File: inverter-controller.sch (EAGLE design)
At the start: 140 parts, among them IC1 STM32F334C8T6, IC10 ISO3082, IC2 SY7152ABC, IC3 LMV358MMX, IC4 LMV358MMX, J1 621006245821, J2 61300211121, X1 0289-9066**15EDGVC-3.81-02P-14, X2 0289-9066**15EDGVC-3.81-02P-14, X3 0289-9068**15EDGVC-3.81-03P-14, X6 1365-16, Y1 NX2016SA-32M

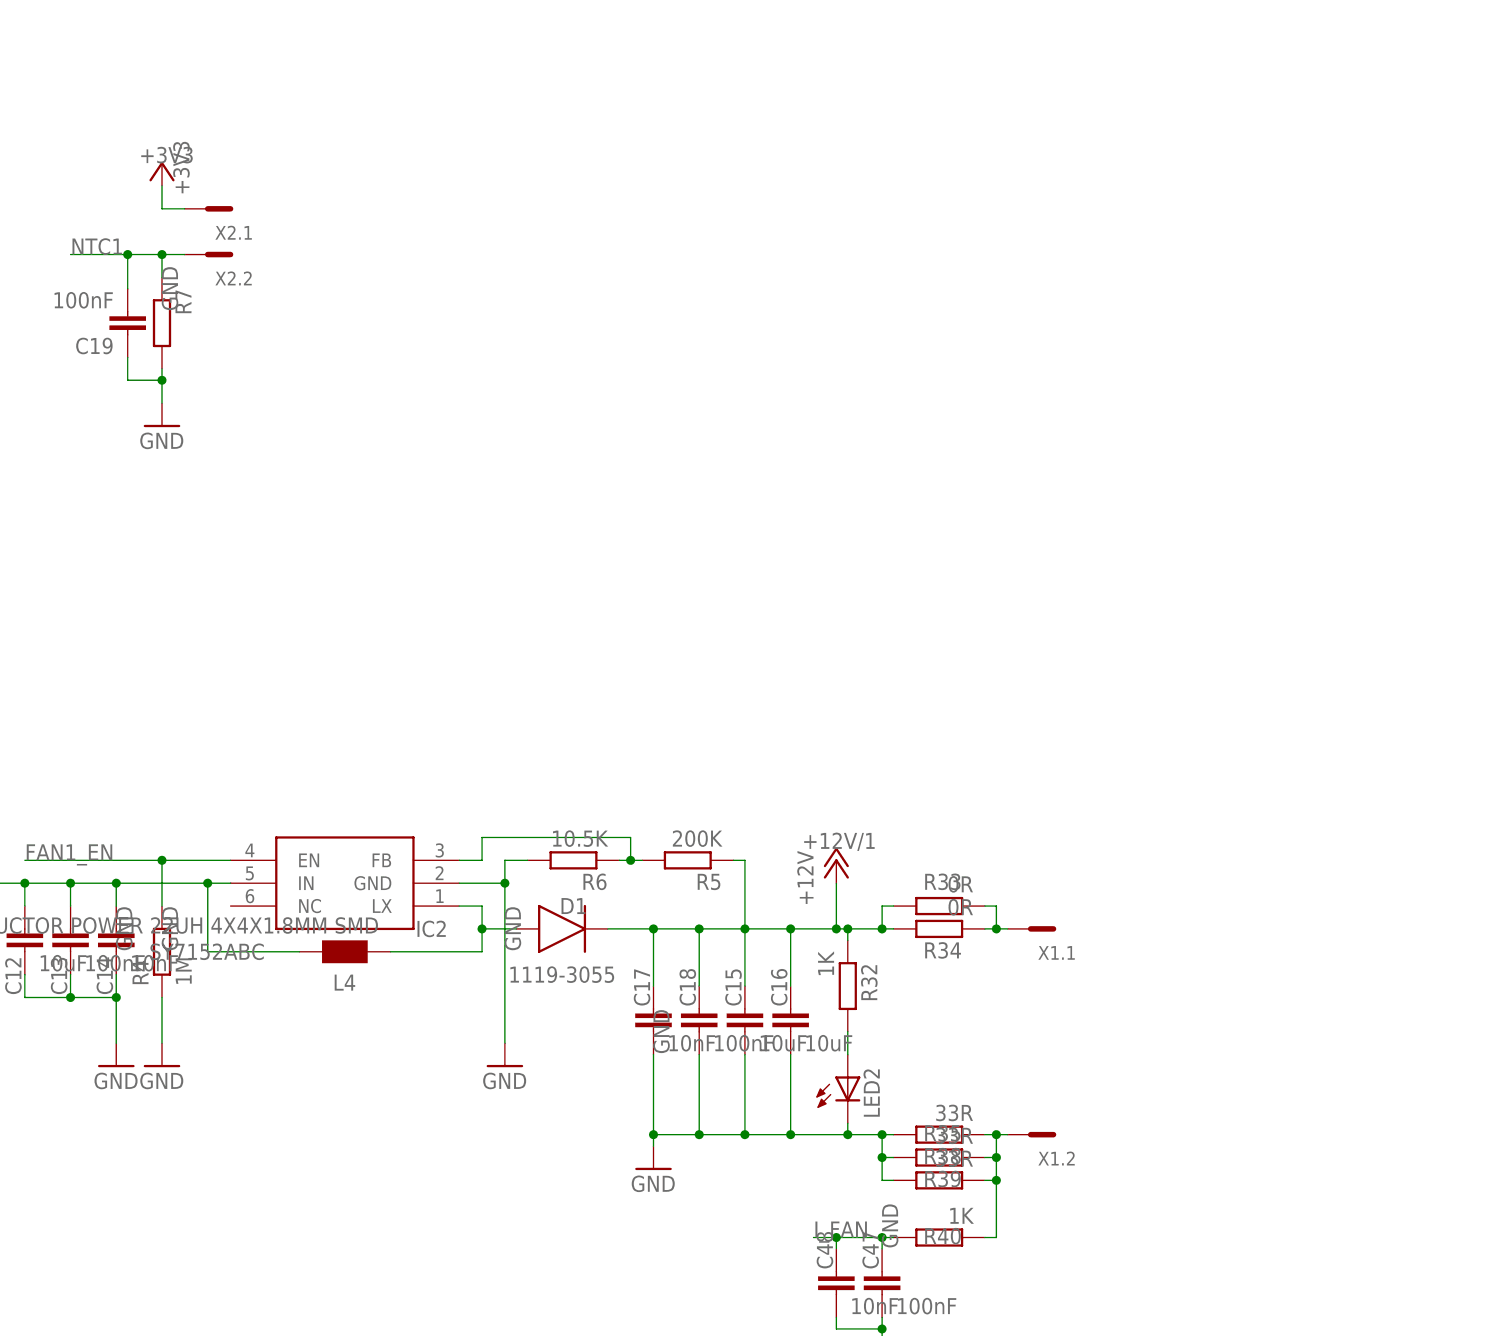
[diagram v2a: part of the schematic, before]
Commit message: Fan ve NTC soketleri SMD-Pad kutuphanesi ile degistirildi.
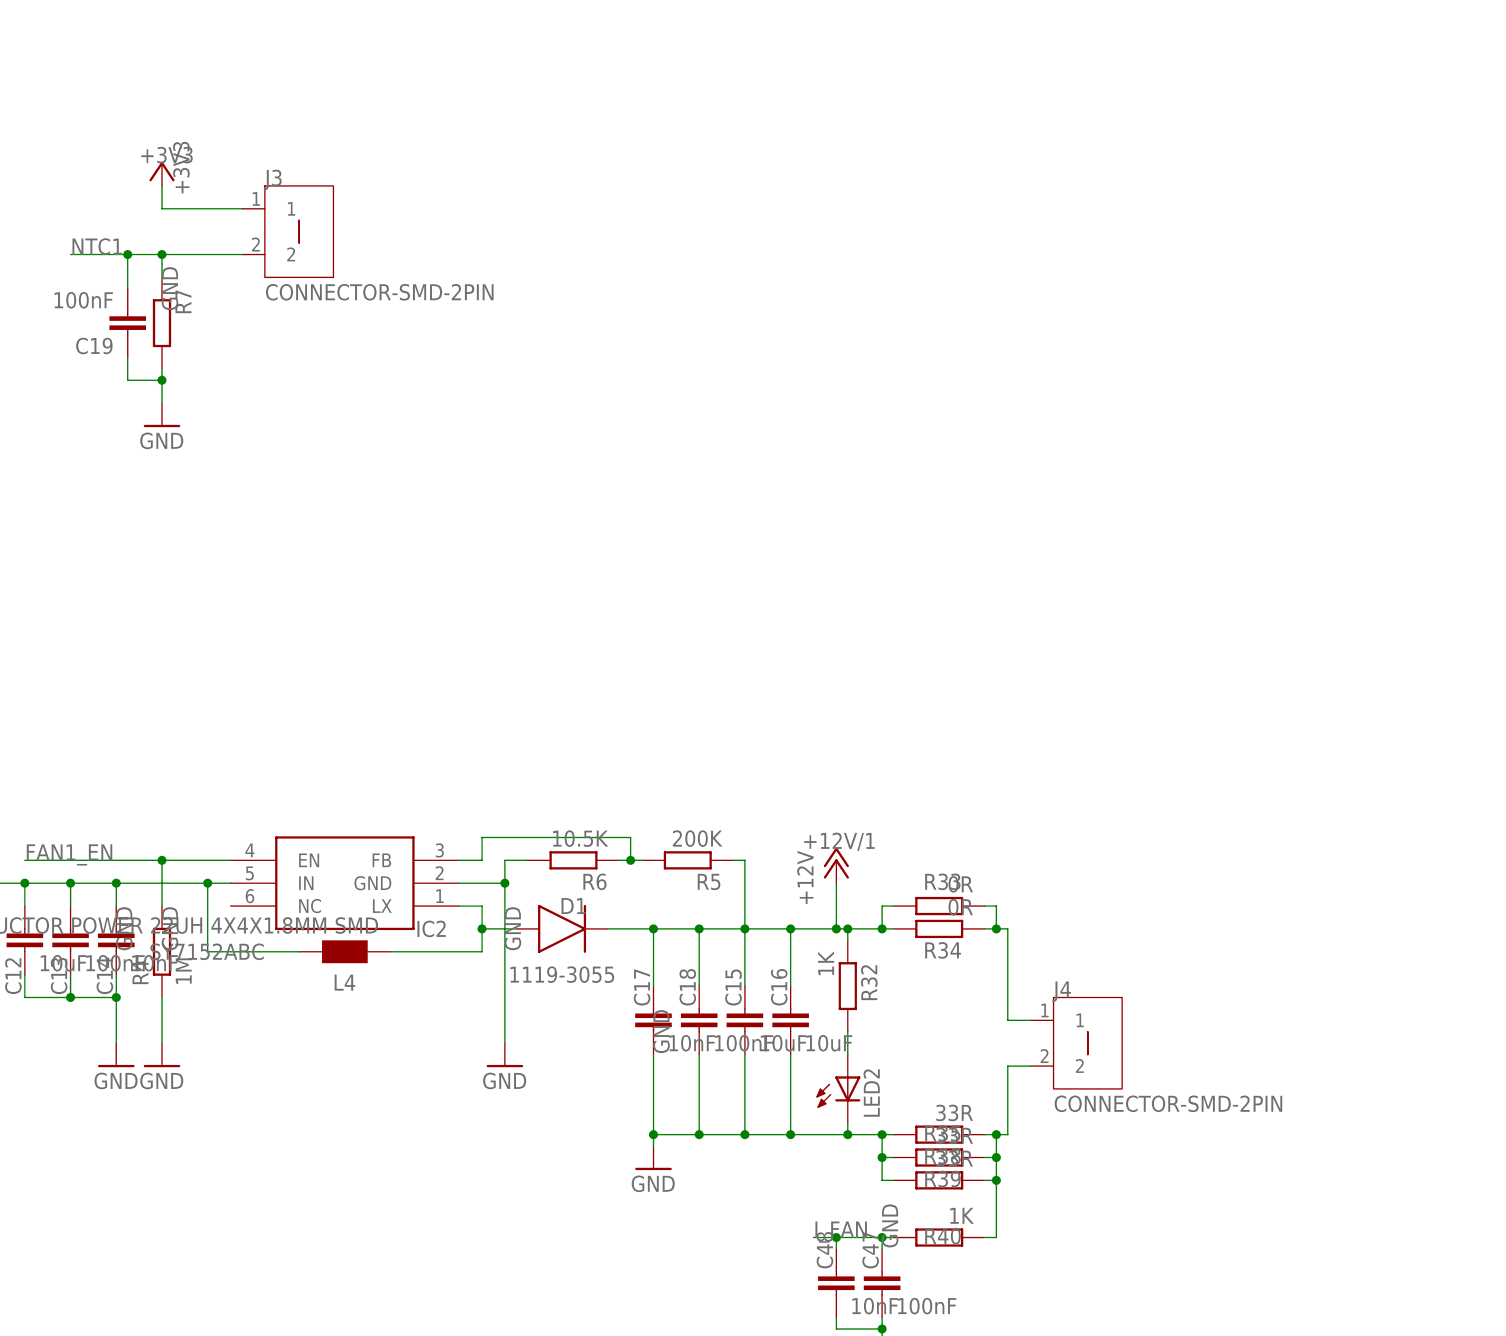
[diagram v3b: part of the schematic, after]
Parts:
- removed X1, X2: 0289-9066**15EDGVC-3.81-02P-14, con-phoenix-381_l:MCV2
- added J3, J4: CONNECTOR-SMD-2PIN, Andromeda:CONNECTOR-SMD-2PIN
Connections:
- net +3V3: now also J3.1; no longer X2.1.SK
- net N$10: now also J4.2; no longer X1.2.SK
- net N$34: now also J4.1; no longer X1.1.SK
- net NTC1: now also J3.2; no longer X2.2.SK
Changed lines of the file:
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@@
 <part name="GND12" library="supply1" library_urn="urn:adsk.eagle:library:371" deviceset="GND" device=""/>
 <part name="P+1" library="supply1" library_urn="urn:adsk.eagle:library:371" deviceset="+12V" device=""/>
-<part name="X1" library="con-phoenix-381_l" deviceset="MCV2" device="" value="0289-9066**15EDGVC-3.81-02P-14"/>
-<part name="X2" library="con-phoenix-381_l" deviceset="MCV2" device="" value="0289-9066**15EDGVC-3.81-02P-14"/>
 <part name="+3V7" library="supply1" library_urn="urn:adsk.eagle:library:371" deviceset="+3V3" device=""/>
 <part name="GND14" library="supply1" library_urn="urn:adsk.eagle:library:371" deviceset="GND" device=""/>
@@
 <part name="+3V17" library="supply1" deviceset="+3V3" device=""/>
 <part name="DC7" library="my_parts1" deviceset="RI-0512S/P_DC_DC_5V_12V" device=""/>
+<part name="J3" library="Andromeda" library_urn="urn:adsk.eagle:library:27258842" deviceset="CONNECTOR-SMD-2PIN" device=""/>
+<part name="J4" library="Andromeda" library_urn="urn:adsk.eagle:library:27258842" deviceset="CONNECTOR-SMD-2PIN" device=""/>
 </parts>
 <sheets>
@@
 <attribute name="VALUE" x="321.31" y="21.59" size="1.778" layer="96" rot="R90"/>
 </instance>
-<instance part="X1" gate=".1" x="342.9" y="19.05" smashed="yes" rot="R180">
-<attribute name="NAME" x="350.52" y="17.145" size="1.524" layer="95" rot="R180"/>
-</instance>
-<instance part="X1" gate=".2" x="342.9" y="-3.81" smashed="yes" rot="R180">
-<attribute name="NAME" x="350.52" y="-5.715" size="1.524" layer="95" rot="R180"/>
-</instance>
-<instance part="X2" gate=".1" x="251.46" y="99.06" smashed="yes" rot="R180">
-<attribute name="NAME" x="259.08" y="97.155" size="1.524" layer="95" rot="R180"/>
-</instance>
-<instance part="X2" gate=".2" x="251.46" y="93.98" smashed="yes" rot="R180">
-<attribute name="NAME" x="259.08" y="92.075" size="1.524" layer="95" rot="R180"/>
-</instance>
 <instance part="+3V7" gate="G$1" x="248.92" y="104.14" smashed="yes">
 <attribute name="VALUE" x="250.19" y="106.68" size="1.778" layer="96" rot="R270"/>
@@
 <attribute name="NAME" x="403.86" y="172.72" size="1.778" layer="95"/>
 <attribute name="VALUE" x="403.86" y="158.75" size="1.778" layer="96"/>
+</instance>
+<instance part="J3" gate="G$1" x="262.89" y="96.52" smashed="yes">
+<attribute name="VALUE" x="260.35" y="88.9" size="1.778" layer="96"/>
+<attribute name="NAME" x="260.35" y="101.6" size="1.778" layer="95"/>
+</instance>
+<instance part="J4" gate="G$1" x="350.52" y="6.35" smashed="yes">
+<attribute name="VALUE" x="347.98" y="-1.27" size="1.778" layer="96"/>
+<attribute name="NAME" x="347.98" y="11.43" size="1.778" layer="95"/>
 </instance>
 </instances>
@@
 </segment>
 <segment>
-<pinref part="X2" gate=".1" pin="SK"/>
-<wire x1="251.46" y1="99.06" x2="248.92" y2="99.06" width="0.1524" layer="91"/>
 <pinref part="+3V7" gate="G$1" pin="+3V3"/>
 <wire x1="248.92" y1="99.06" x2="248.92" y2="101.6" width="0.1524" layer="91"/>
 <label x="246.38" y="104.14" size="1.778" layer="95"/>
+<pinref part="J3" gate="G$1" pin="1"/>
+<wire x1="248.92" y1="99.06" x2="257.81" y2="99.06" width="0.1524" layer="91"/>
 </segment>
 <segment>
@@
 </segment>
 <segment>
-<pinref part="X2" gate=".2" pin="SK"/>
-<wire x1="251.46" y1="93.98" x2="248.92" y2="93.98" width="0.1524" layer="91"/>
 <wire x1="248.92" y1="93.98" x2="245.11" y2="93.98" width="0.1524" layer="91"/>
 <wire x1="245.11" y1="93.98" x2="238.76" y2="93.98" width="0.1524" layer="91"/>
@@
 <junction x="248.92" y="93.98"/>
 <pinref part="C19" gate="G$1" pin="2"/>
+<pinref part="J3" gate="G$1" pin="2"/>
+<wire x1="248.92" y1="93.98" x2="257.81" y2="93.98" width="0.1524" layer="91"/>
 </segment>
 </net>
@@
 <net name="N$34" class="0">
 <segment>
-<pinref part="X1" gate=".1" pin="SK"/>
 <wire x1="340.36" y1="19.05" x2="341.63" y2="19.05" width="0.1524" layer="91"/>
 <wire x1="341.63" y1="19.05" x2="342.9" y2="19.05" width="0.1524" layer="91"/>
@@
 <pinref part="R33" gate="G$1" pin="1"/>
 <pinref part="R34" gate="G$1" pin="1"/>
+<wire x1="342.9" y1="19.05" x2="342.9" y2="8.89" width="0.1524" layer="91"/>
+<pinref part="J4" gate="G$1" pin="1"/>
+<wire x1="342.9" y1="8.89" x2="345.44" y2="8.89" width="0.1524" layer="91"/>
 </segment>
 </net>
 <net name="N$10" class="0">
 <segment>
-<pinref part="X1" gate=".2" pin="SK"/>
 <wire x1="340.36" y1="-3.81" x2="341.63" y2="-3.81" width="0.1524" layer="91"/>
 <wire x1="341.63" y1="-3.81" x2="342.9" y2="-3.81" width="0.1524" layer="91"/>
@@
 <pinref part="R39" gate="G$1" pin="1"/>
 <pinref part="R40" gate="G$1" pin="1"/>
-</segment>
-</net>
+<pinref part="J4" gate="G$1" pin="2"/>
+<wire x1="345.44" y1="3.81" x2="342.9" y2="3.81" width="0.1524" layer="91"/>
+<wire x1="342.9" y1="3.81" x2="342.9" y2="-3.81" width="0.1524" layer="91"/>
+</segment>
+</net>

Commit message: 485 pinleri degistirildi, analog-girisler icin aciklama eklendi.
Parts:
- added C54, C59, C62: 10uF, rcl:C-EUC0603E
- added C55, C58, C63: 100nF, rcl:C-EUC0603E
- added C56, C57, C64: 10nF, rcl:C-EUC0603E
- added D5: 1119-3055, Diode:DIODEDO-214AC(SMA)
- added IC5: SY7152ABC, SY7152ABC:SY7152ABC
- added J5: CONNECTOR-SMD-2PIN, Andromeda:CONNECTOR-SMD-2PIN
- added L2: 1319-4102**INDUCTOR POWER 22UH 4X4X1.8MM SMD, wuerth-elektronik:WE-PD2_S
- added LED3: (no value), adafruit:LEDCHIP-LED0805
- added R42: 1M, rcl:R-EU_R0603E
- added R43: 200K, rcl:R-EU_R0603E
- added R44: 10.5K, rcl:R-EU_R0603E
- added R45, R46: 0R, rcl:R-EU_R0603E
- added R47, R55: 1K, rcl:R-EU_R0603E
- added R49, R50, R53: 33R, rcl:R-EU_R0603E
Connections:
- new net +12V/2: C57.1, C58.1, C59.1, C62.1, D5.C, R43.1, R45.2, R46.2, R47.1
- new net FAN2_EN: IC1.PB13, IC5.EN, R42.2
- new net I_FAN1: C47.1, C48.1, R40.2
- new net N$25: D5.A, IC5.LX, L2.1
- new net N$26: IC5.FB, R43.2, R44.1
- new net N$27: J5.1, R45.1, R46.1
- new net N$28: J5.2, R49.1, R50.1, R53.1, R55.1
- new net N$29: LED3.A, R47.2
- net +3V3: now also C54.1, C55.1, C56.1, IC5.IN, L2.2
- net GND: now also C54.2, C55.2, C56.2, C57.2, C58.2, C59.2, C62.2, C63.2, C64.2, IC5.GND, LED3.C, R42.1, R44.2, R49.2, R50.2, R53.2
- net I_FAN: now also C63.1, C64.1, R55.2; no longer C47.1, C48.1, R40.2
- net RS485_RX: now also IC1.PB7; no longer IC1.PB11
- net RS485_TX: now also IC1.PB6; no longer IC1.PB10
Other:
- note added: "/ADC2_IN13"
- note added: "/ADC2_IN14"
- note added: "/ADC2_IN15"
- note added: "ADC1_IN11/"
- note added: "ADC1_IN12/"
- note added: "ADC2_IN12/"

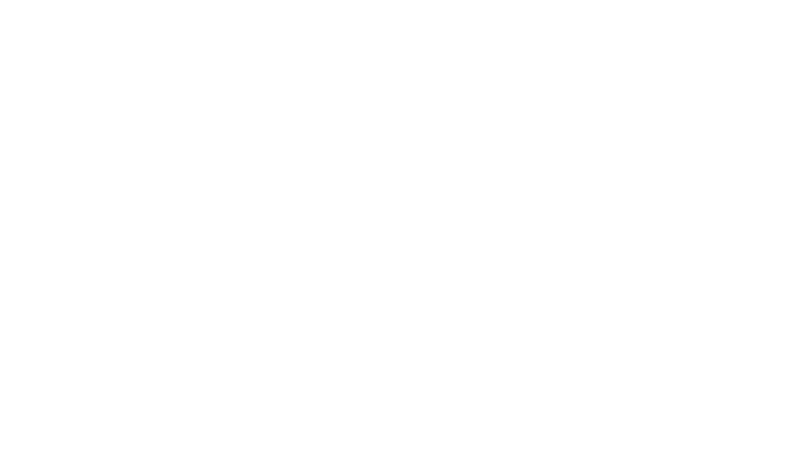
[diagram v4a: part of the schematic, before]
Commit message: Kart baglanti pad'leri eklendi.
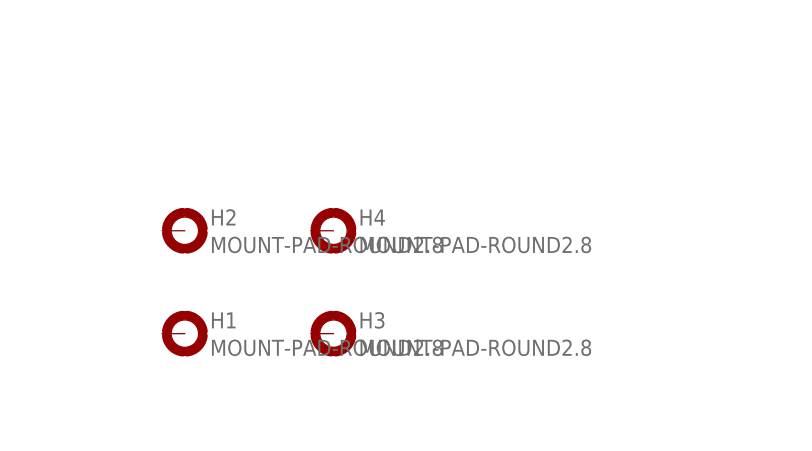
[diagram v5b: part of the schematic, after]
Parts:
- added H1, H2, H3, H4: MOUNT-PAD-ROUND2.8, holes:MOUNT-PAD-ROUND2.8
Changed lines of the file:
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@@
 <part name="C64" library="rcl" library_urn="urn:adsk.eagle:library:26637914" deviceset="C-EU" device="C0603E" package3d_urn="urn:adsk.eagle:package:26638827/1" value="10nF"/>
 <part name="J5" library="Andromeda" library_urn="urn:adsk.eagle:library:27258842" deviceset="CONNECTOR-SMD-2PIN" device=""/>
+<part name="H1" library="holes" library_urn="urn:adsk.eagle:library:237" deviceset="MOUNT-PAD-ROUND" device="2.8" package3d_urn="urn:adsk.eagle:package:14281/1"/>
+<part name="H2" library="holes" library_urn="urn:adsk.eagle:library:237" deviceset="MOUNT-PAD-ROUND" device="2.8" package3d_urn="urn:adsk.eagle:package:14281/1"/>
+<part name="H3" library="holes" library_urn="urn:adsk.eagle:library:237" deviceset="MOUNT-PAD-ROUND" device="2.8" package3d_urn="urn:adsk.eagle:package:14281/1"/>
+<part name="H4" library="holes" library_urn="urn:adsk.eagle:library:237" deviceset="MOUNT-PAD-ROUND" device="2.8" package3d_urn="urn:adsk.eagle:package:14281/1"/>
 </parts>
 <sheets>
@@
 <attribute name="NAME" x="500.38" y="10.16" size="1.778" layer="95"/>
 </instance>
+<instance part="H1" gate="G$1" x="41.91" y="-21.59" smashed="yes">
+<attribute name="NAME" x="44.704" y="-21.0058" size="1.778" layer="95"/>
+<attribute name="VALUE" x="44.704" y="-24.0538" size="1.778" layer="96"/>
+</instance>
+<instance part="H2" gate="G$1" x="41.91" y="-10.16" smashed="yes">
+<attribute name="NAME" x="44.704" y="-9.5758" size="1.778" layer="95"/>
+<attribute name="VALUE" x="44.704" y="-12.6238" size="1.778" layer="96"/>
+</instance>
+<instance part="H3" gate="G$1" x="58.42" y="-21.59" smashed="yes">
+<attribute name="NAME" x="61.214" y="-21.0058" size="1.778" layer="95"/>
+<attribute name="VALUE" x="61.214" y="-24.0538" size="1.778" layer="96"/>
+</instance>
+<instance part="H4" gate="G$1" x="58.42" y="-10.16" smashed="yes">
+<attribute name="NAME" x="61.214" y="-9.5758" size="1.778" layer="95"/>
+<attribute name="VALUE" x="61.214" y="-12.6238" size="1.778" layer="96"/>
+</instance>
 </instances>

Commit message: Fan Controller-2 yerleşimi yapıldı
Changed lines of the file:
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@@
 </instances>
 <busses>
+<bus name="B$1">
+<segment>
+<wire x1="250.19" y1="121.92" x2="273.05" y2="121.92" width="0.762" layer="92"/>
+<wire x1="273.05" y1="121.92" x2="273.05" y2="55.88" width="0.762" layer="92"/>
+</segment>
+</bus>
+<bus name="B$2">
+<segment>
+<wire x1="250.19" y1="275.59" x2="281.94" y2="275.59" width="0.762" layer="92"/>
+<wire x1="281.94" y1="275.59" x2="281.94" y2="129.54" width="0.762" layer="92"/>
+</segment>
+</bus>
+<bus name="B$3">
+<segment>
+<wire x1="436.88" y1="276.86" x2="467.36" y2="276.86" width="0.762" layer="92"/>
+<wire x1="467.36" y1="276.86" x2="467.36" y2="127" width="0.762" layer="92"/>
+</segment>
+</bus>
+<bus name="B$4">
+<segment>
+<wire x1="78.74" y1="270.51" x2="105.41" y2="270.51" width="0.762" layer="92"/>
+<wire x1="105.41" y1="270.51" x2="105.41" y2="168.91" width="0.762" layer="92"/>
+</segment>
+</bus>
+<bus name="B$5">
+<segment>
+<wire x1="66.04" y1="157.48" x2="96.52" y2="157.48" width="0.762" layer="92"/>
+<wire x1="96.52" y1="157.48" x2="96.52" y2="-1.27" width="0.762" layer="92"/>
+</segment>
+</bus>
 </busses>
 <nets>
